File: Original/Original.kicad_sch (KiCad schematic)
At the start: 49 parts, among them J1 QL_SLOT_DIN41612, J2 Conn_02x17_Odd_Even, J3 -, J4 +, J5 nc, J6 nc, Q1 BC109, U0 LM340T-5, U1 68000D, U10 MSM514400D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

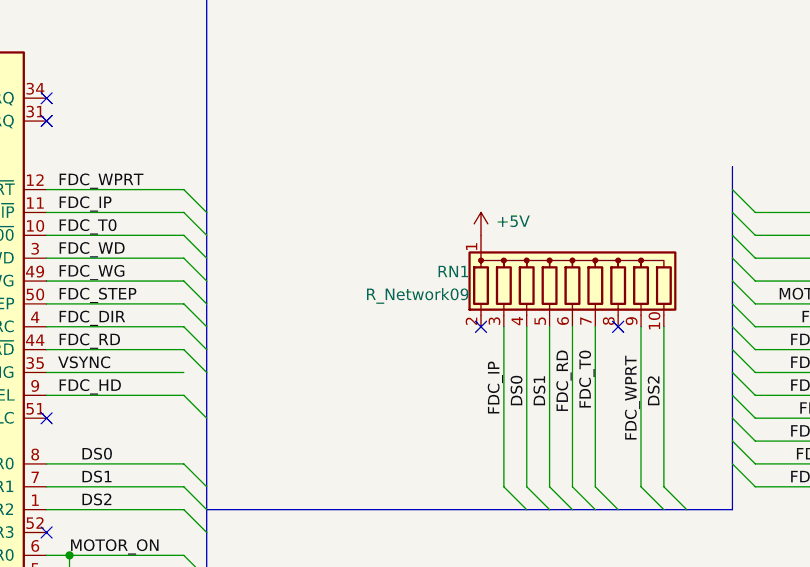
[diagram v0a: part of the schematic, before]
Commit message: remove last extra vias
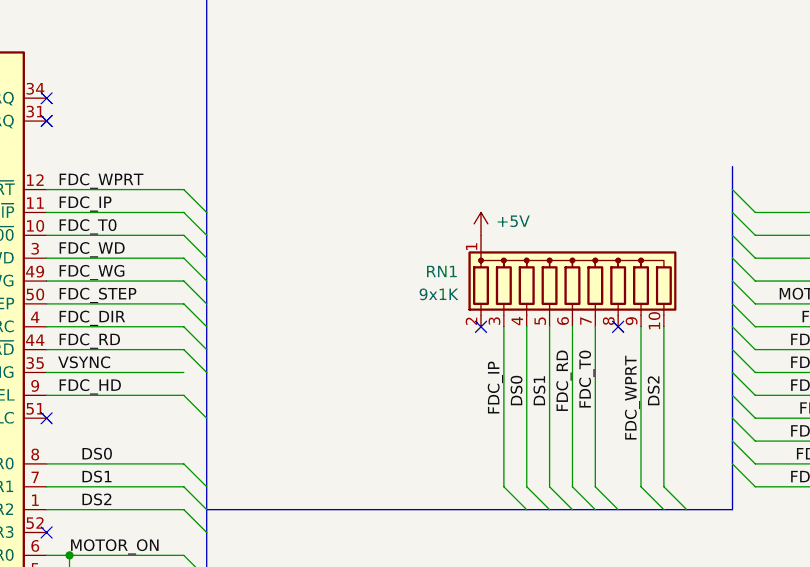
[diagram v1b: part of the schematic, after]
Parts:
- RN1: value R_Network09 -> 9x1K
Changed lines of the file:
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@@
 		(fields_autoplaced yes)
 		(property "Reference" "RN1"
-			(at 147.32 92.964 0)
+			(at 146.05 92.9639 0)
 			(effects
 				(font
@@
 			)
 		)
-		(property "Value" "R_Network09"
-			(at 147.32 95.504 0)
+		(property "Value" "9x1K"
+			(at 146.05 95.5039 0)
 			(effects
 				(font

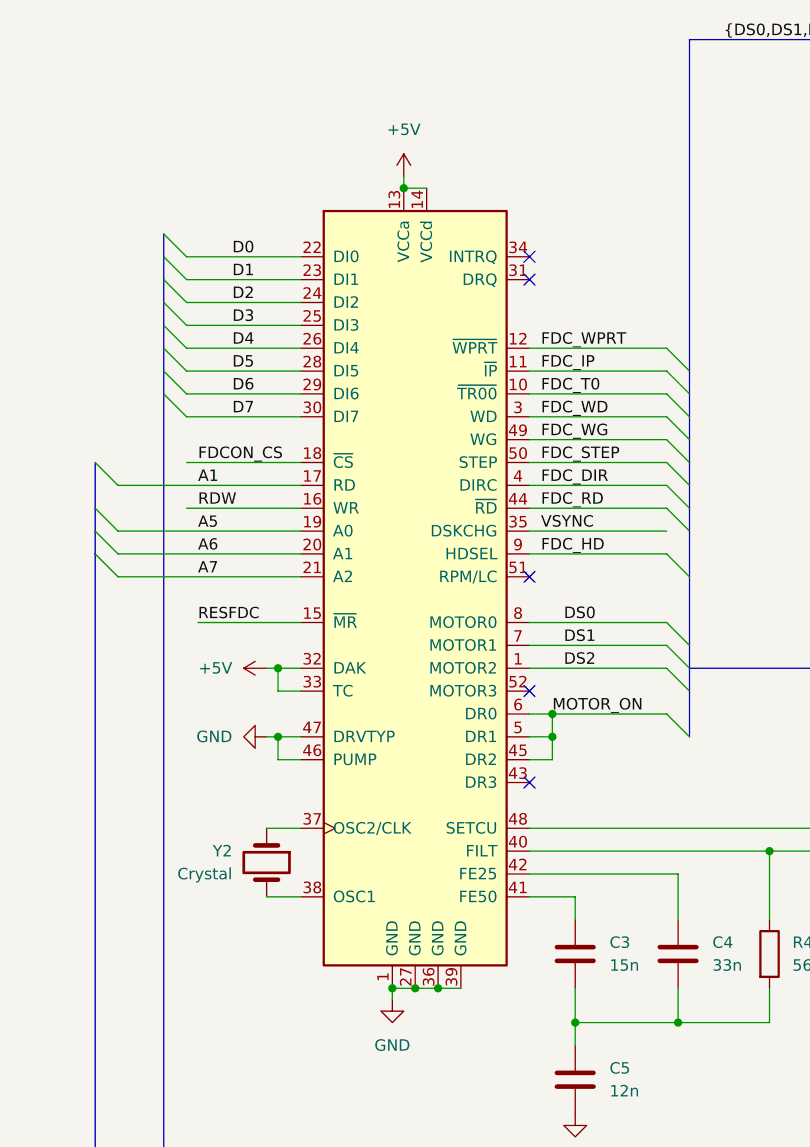
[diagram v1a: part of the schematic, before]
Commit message: update again for bad FDC pinout
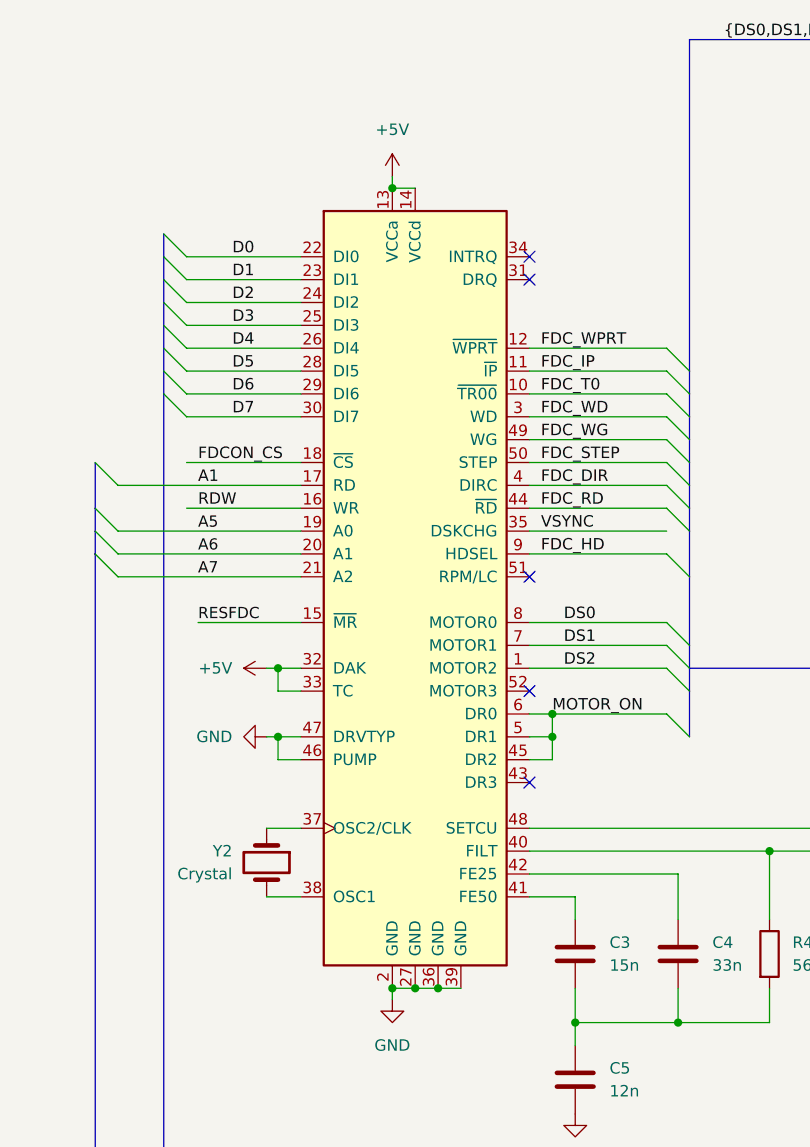
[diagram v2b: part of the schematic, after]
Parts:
- U12: footprint Package_LCC:PLCC-52_THT-Socket -> Package_LCC:PLCC-52*
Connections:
- net GND: now also U12.2 (GND); no longer U12.1 (MOTOR2)
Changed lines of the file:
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@@
 	)
 	(junction
+		(at 85.09 66.04)
+		(diameter 0)
+		(color 0 0 0 0)
+	)
+	(junction
 		(at 209.55 109.22)
 		(diameter 0)
@@
 		(color 0 0 0 0)
 	)
-	(junction
-		(at 86.36 66.04)
-		(diameter 0)
-		(color 0 0 0 0)
-	)
 	(no_connect
 		(at 118.11 254)
@@
 	(wire
 		(pts
-			(xy 86.36 64.77) (xy 86.36 66.04)
+			(xy 85.09 64.77) (xy 85.09 66.04)
 		)
 		(stroke
@@
 	(wire
 		(pts
-			(xy 86.36 66.04) (xy 88.9 66.04)
+			(xy 85.09 66.04) (xy 87.63 66.04)
 		)
 		(stroke
@@
 	(symbol
 		(lib_id "GoldCard_Library:+5V")
-		(at 86.36 64.77 0)
+		(at 85.09 64.77 0)
 		(unit 1)
 		(exclude_from_sim no)
@@
 		(fields_autoplaced yes)
 		(property "Reference" "#PWR038"
-			(at 86.36 68.58 0)
+			(at 85.09 68.58 0)
 			(effects
 				(font
@@
 		)
 		(property "Value" "+5V"
-			(at 86.36 59.5376 0)
+			(at 85.09 59.5376 0)
 			(effects
 				(font
@@
 		)
 		(property "Footprint" ""
-			(at 86.36 64.77 0)
+			(at 85.09 64.77 0)
 			(effects
 				(font
@@
 		)
 		(property "Datasheet" ""
-			(at 86.36 64.77 0)
+			(at 85.09 64.77 0)
 			(effects
 				(font
@@
 		)
 		(property "Description" ""
-			(at 86.36 64.77 0)
+			(at 85.09 64.77 0)
 			(effects
 				(font
@@
 			)
 		)
-		(property "Footprint" "Package_LCC:PLCC-52_THT-Socket"
+		(property "Footprint" "Package_LCC:PLCC-52*"
 			(at 106.68 129.54 0)
 			(effects
@@
 		(pin "21"
 		)
-		(pin "1"
+		(pin "2"
 		)
 		(pin "10"

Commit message: fix values
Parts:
- C1, C2: value C -> 22p
- C7: value 330n -> 100n
- Q1: value BC109 -> BC548
- R1, R2: value R -> 1k
- U12: footprint Package_LCC:PLCC-52* -> Package_LCC:PLCC-52_THT-Socket
- Y3: value Crystal -> 32768Hz
- renumbered C10 to C16, C16 to C17
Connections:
- net GND: now also U6.18 (B0); no longer C7.2
- net at D1.2 (A), D2.2 (A), U7.8 (GND): now also C7.2
- no-connect marks 45 -> 44
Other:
- moved on the sheet: C16
